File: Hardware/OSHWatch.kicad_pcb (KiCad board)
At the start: 4 copper layers, 30 x 36 mm, 46 parts, among them P1 CONN_30, U1 SPBT2632C2A.AT2, U10 DRV2605L, U2 STM32F072, U3 MCP73831T, U4 FAN5331, U5 TPS61200

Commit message: Initial layout complete
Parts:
- added C15: 22uF, SM0603, F.Cu at (30.9, 45.2)
- added C25: 100nF, SM0402, F.Cu at (17.5, 24.9)
- added C26: 1uF, SM0402, B.Cu at (40.9, 42.7)
- added CON1: USB-MINI-B, 10118192, F.Cu at (19.4, 52.2)
- added D1: 1N4148, SOD-523, B.Cu at (28.6, 30.7)
- added D2: 1N4148, SOD-523, B.Cu at (28.6, 29.3)
- added D3: BAT54T1G, SOD-123, B.Cu at (29.2, 19.4)
- added L1: 10uH, 2518, B.Cu at (33.1, 22.0)
- added L2: 4.7uH, 1.2A, 2518, F.Cu at (27.2, 42.0)
- added M1: DC_MOTOR, 2PAD, B.Cu at (39.2, 49.1)
- added OSC1: KD3270031, KD3270031, F.Cu at (38.6, 20.6)
- added P2: CONN_2, 2PAD, B.Cu at (29.6, 50.9)
- added P3: CONN_4, 4pin, F.Cu at (29.6, 52.7)
- added R17: 10K, SM0402, B.Cu at (28.3, 24.8)
- added R18: 10K, SM0402, B.Cu at (31.1, 16.0)
- added R19: 200k, SM0402, F.Cu at (19.3, 15.2)
- added R20: 10K, SM0402, F.Cu at (17.4, 37.8)
- added R21: 200k, SM0402, B.Cu at (40.9, 46.7)
- added R22: 200k, SM0402, B.Cu at (42.9, 45.7)
- added R23: 10K, SM0402, F.Cu at (16.6, 18.2)
- added R24: 10K, SM0402, F.Cu at (38.9, 15.6)
- added R25: 10K, SM0402, B.Cu at (35.2, 48.4)
- added R26: 10K, SM0402, F.Cu at (15.5, 18.2)
- added R27: 10K, SM0402, F.Cu at (37.6, 15.6)
- added R28: 10K, SM0402, B.Cu at (34.2, 48.4)
- added SW1: SW_PUSH, B3U-3000P, B.Cu at (18.5, 15.5)
- added SW2: SW_PUSH, B3U-3000P, B.Cu at (39.4, 15.5)
- added SW3: SW_PUSH, B3U-3000P, F.Cu at (39.5, 52.5)
- added U11: BMP280, BMP280, F.Cu at (16.6, 27.8)
- added U6: ML8511, ML8511, F.Cu at (22.9, 16.8)
- added U7: APDS-9960, APDS-9960, F.Cu at (29.5, 16.3)
- added U8: LSM9DS0, LSM9DS0, F.Cu at (20.4, 39.2)
- added U9: HTU21DF, HTU12DF, F.Cu at (20.6, 25.4)
- C1, C12, C14, C19, R13, R16, U10: moved to B.Cu
- C16: value 10uf -> 100uF; footprint SM0402 -> SM0805; moved to B.Cu
- C18: value 1uf -> 1nF
- C23: value 1uf -> 100nF
- C24: value 1uf -> 0.1uF; moved to B.Cu
- moved C21 34.2 mm to (22.6, 42.0)
- moved C10 33.6 mm to (15.6, 47.0), turned to 180 degrees
- moved R14 32.7 mm to (30.6, 47.2), turned to 180 degrees
- moved R1 32.3 mm to (16.6, 33.0)
- moved R2 31.7 mm to (18.3, 31.6)
- moved C24 30.8 mm to (36.8, 47.0), turned to 270 degrees
- moved C20 30.5 mm to (17.4, 39.6), turned to 270 degrees
- moved C13 29.8 mm to (30.5, 43.1)
- moved C11 27.4 mm to (26.3, 49.8), turned to 180 degrees
- moved R9 26.8 mm to (26.3, 48.6), turned to 180 degrees
- moved C22 26.4 mm to (20.7, 42.0), turned to 180 degrees
- moved U2 26.2 mm to (26.8, 33.0), turned to 270 degrees
- moved C23 24.9 mm to (15.9, 25.3), turned to 90 degrees
- moved C1 24.6 mm to (42.9, 40.9), turned to 270 degrees
- moved U4 19.1 mm to (29.6, 22.0), turned to 270 degrees
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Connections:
- C16 pad 1: +3.3V -> +BATT
- C19 pad 1: +3.3V -> +BATT
- R16 pad 1: N-00000104 -> N-0000027
- R16 pad 2: +3.3V -> /Bluetooth/BT_RESET
- R6 pad 1: +BATT -> N-0000028
- R6 pad 2: /Power/VBAT_SENSE -> /Bluetooth/32KHZ_CLK
- R7 pad 1: /Power/VBAT_SENSE -> N-0000028
- U1 pad 10: /Bluetooth/BT_RESET -> N-0000027
- U1 pad 11: /Bluetooth/BT_CTS_STM_RTS -> (no net)
- U1 pad 12: /Bluetooth/BT_RTS_STM_CTS -> (no net)
- U1 pad 15: (no net) -> N-0000028
- U2 pad 10: /Bluetooth/BT_RX_STM_TX -> /STM32F072/BUTTON_1
- U2 pad 11: /Bluetooth/BT_TX_STM_RX -> /STM32F072/UV_EN
- U2 pad 12: (no net) -> /Power/DISPLAY_BIAS_EN
- U2 pad 19: /STM32F072/GESTURE_INT -> /Display/DISPLAY_DC
- U2 pad 2: (no net) -> /STM32F072/GESTURE_INT
- U2 pad 20: /STM32F072/GYRO_INT -> /Display/DISPLAY_RESET
- U2 pad 28: (no net) -> /STM32F072/GYRO_INT
- U2 pad 29: /Power/DISPLAY_BIAS_EN -> /STM32F072/XM_INT
- U2 pad 34: (no net) -> N-0000041
- U2 pad 37: (no net) -> N-0000042
- U2 pad 38: /Bluetooth/BT_CTS_STM_RTS -> /STM32F072/BUTTON_3
- U2 pad 39: /Display/DISPLAY_RESET -> /STM32F072/BUTTON_2
- U2 pad 40: /Display/DISPLAY_DC -> (no net)
- U2 pad 41: /STM32F072/XM_INT -> (no net)
- U2 pad 42: /STM32F072/UV_EN -> /Bluetooth/BT_RX_STM_TX
- U2 pad 43: /Bluetooth/BT_RTS_STM_CTS -> /Bluetooth/BT_TX_STM_RX
- U2 pad 7: (no net) -> /STM32F072/NRST
- U4 pad 4: /Power/DISPLAY_BIAS_EN -> N-0000086
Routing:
- net +BATT: track 0.00 -> 117.7 mm, vias 0 -> 8
- net /STM32F072/I2C_SCK: track 0.00 -> 74.0 mm, vias 0 -> 4
- net /STM32F072/I2C_SDA: track 0.00 -> 67.7 mm, vias 0 -> 6
- net +3.3V: track 0.00 -> 60.8 mm, vias 0 -> 22
- net /STM32F072/NRST: track 0.00 -> 33.1 mm, vias 0 -> 1
- net /STM32F072/VIB_TRIG: track 0.00 -> 32.7 mm, vias 0 -> 2
- net /Bluetooth/BT_RESET: track 0.00 -> 30.0 mm, vias 0 -> 3
- net /STM32F072/BUTTON_2: track 0.00 -> 26.1 mm, vias 0 -> 2
- net /STM32F072/VIB_EN: track 0.00 -> 25.1 mm, vias 0 -> 2
- net /STM32F072/UV_OUT: track 0.00 -> 23.2 mm, vias 0 -> 2
- net /STM32F072/UV_EN: track 0.00 -> 21.1 mm, vias 0 -> 2
- net GND: track 0.00 -> 21.1 mm, vias 0 -> 8
- net /STM32F072/BUTTON_3: track 0.00 -> 20.7 mm, vias 0 -> 2
- net N-0000042: track 0.00 -> 20.6 mm, vias 0 -> 2
- net N-0000041: track 0.00 -> 19.6 mm
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- added copper zone on Inner1.Cu, net GND
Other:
- board size 30 x 36 mm -> 30 x 39.9 mm
- net class Default: trace_width 0.254 -> 0.2032; via_dia 0.889 -> 0.635; via_drill 0.635 -> 0.3048
- net class Power added: clearance 0.2, trace_width 0.254, via_dia 0.635, via_drill 0.3048
- rule trace_min: 0.254 -> 0.127
- rule via_min_drill: 0.508 -> 0.3048
- rule via_min_size: 0.889 -> 0.635

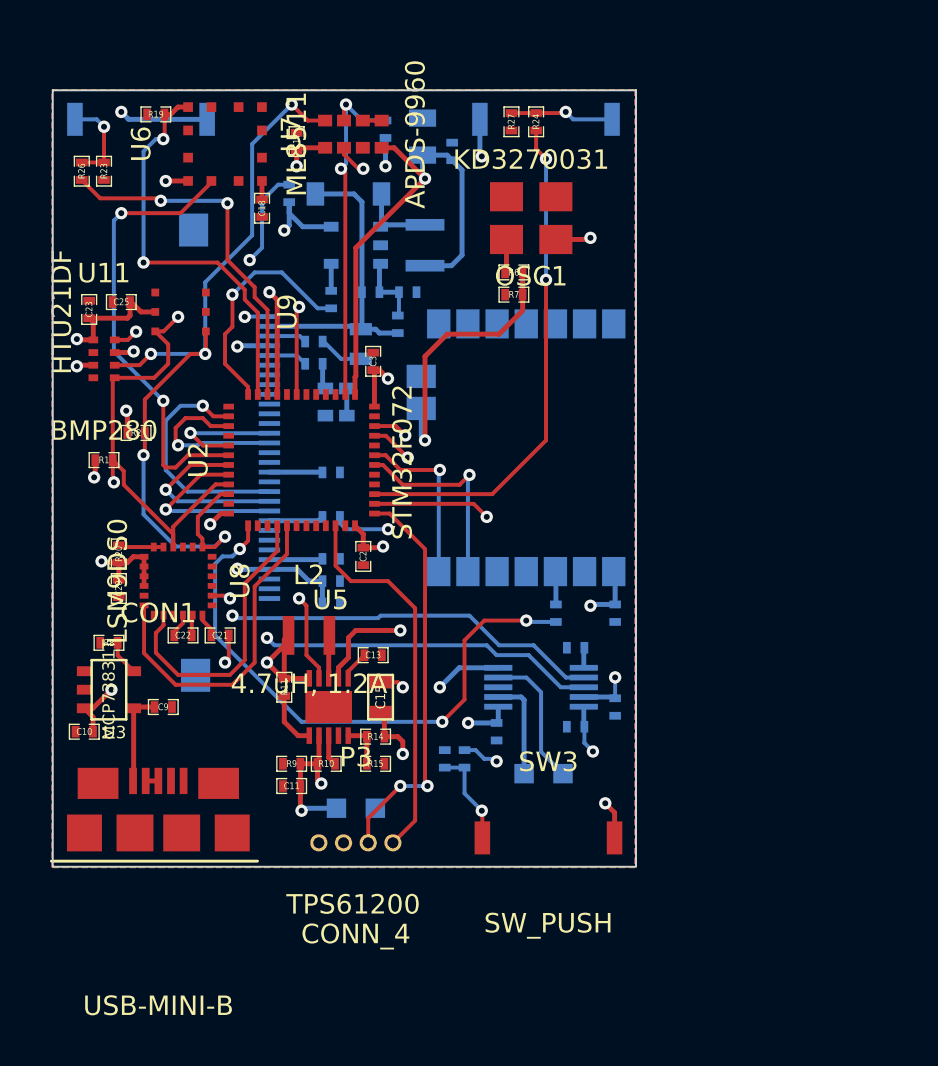
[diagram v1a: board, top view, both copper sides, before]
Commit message: Footprint corrections
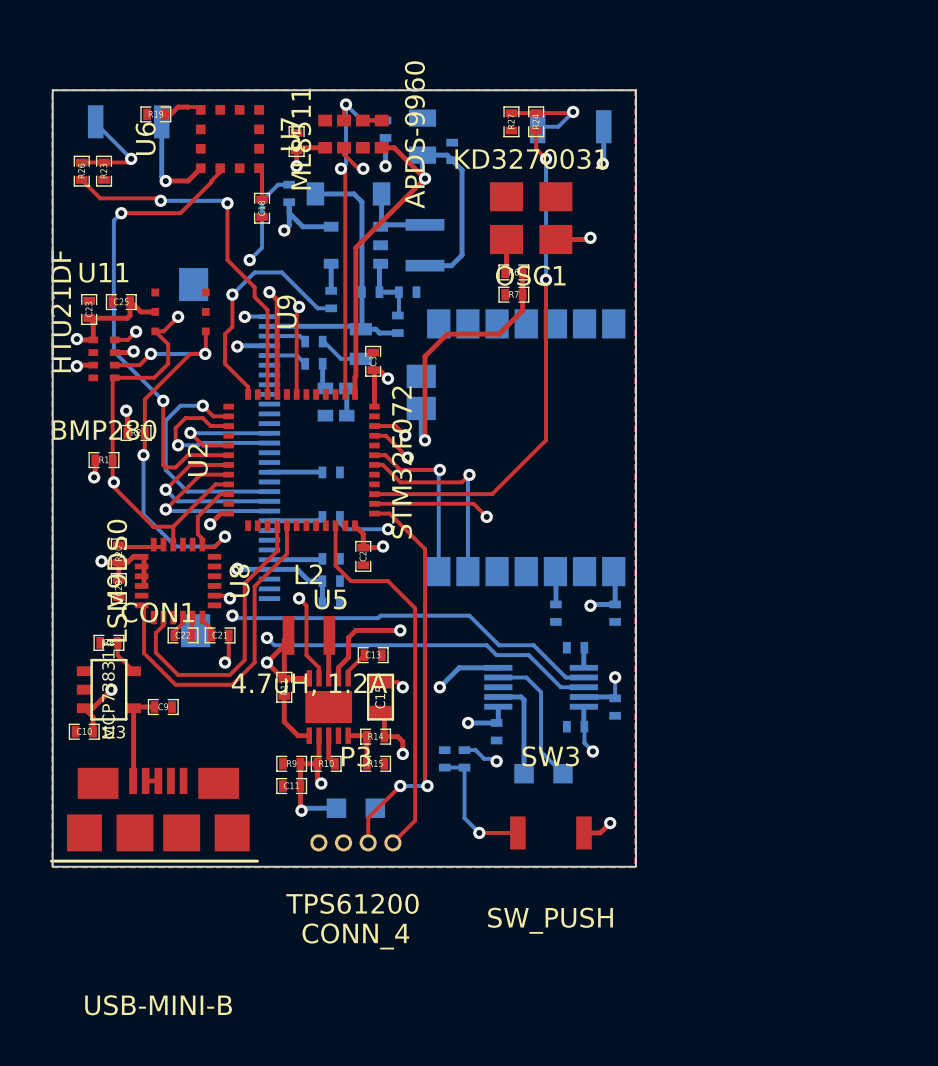
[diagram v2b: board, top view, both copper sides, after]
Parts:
- moved SW2 1.33 mm to (40.6, 15.9), turned to 180 degrees
- moved SW1 0.65 mm to (17.9, 15.6)
- moved U6 0.36 mm to (23.1, 16.5)
- moved SW3 0.28 mm to (39.6, 52.2)
- moved P1 0.25 mm to (25.1, 32.9)
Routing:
- net /Bluetooth/BT_RESET: track 30.0 -> 0.00 mm, vias 3 -> 0
- net /STM32F072/UV_EN: track 21.1 -> 2.08 mm, vias 2 -> 0
- net /STM32F072/I2C_SDA: track 67.7 -> 50.9 mm, vias 6 -> 5
- net N-0000099: track 5.01 -> 6.68 mm
- net /STM32F072/I2C_SCK: track 74.0 -> 72.4 mm
- net +3.3V: track 60.8 -> 59.8 mm, vias 22 -> 21
- net /STM32F072/UV_OUT: track 23.2 -> 24.0 mm
- net N-0000095: track 0.95 -> 1.67 mm
- net N-00000100: track 4.63 -> 5.28 mm

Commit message: Final footprint corrections, gerbers
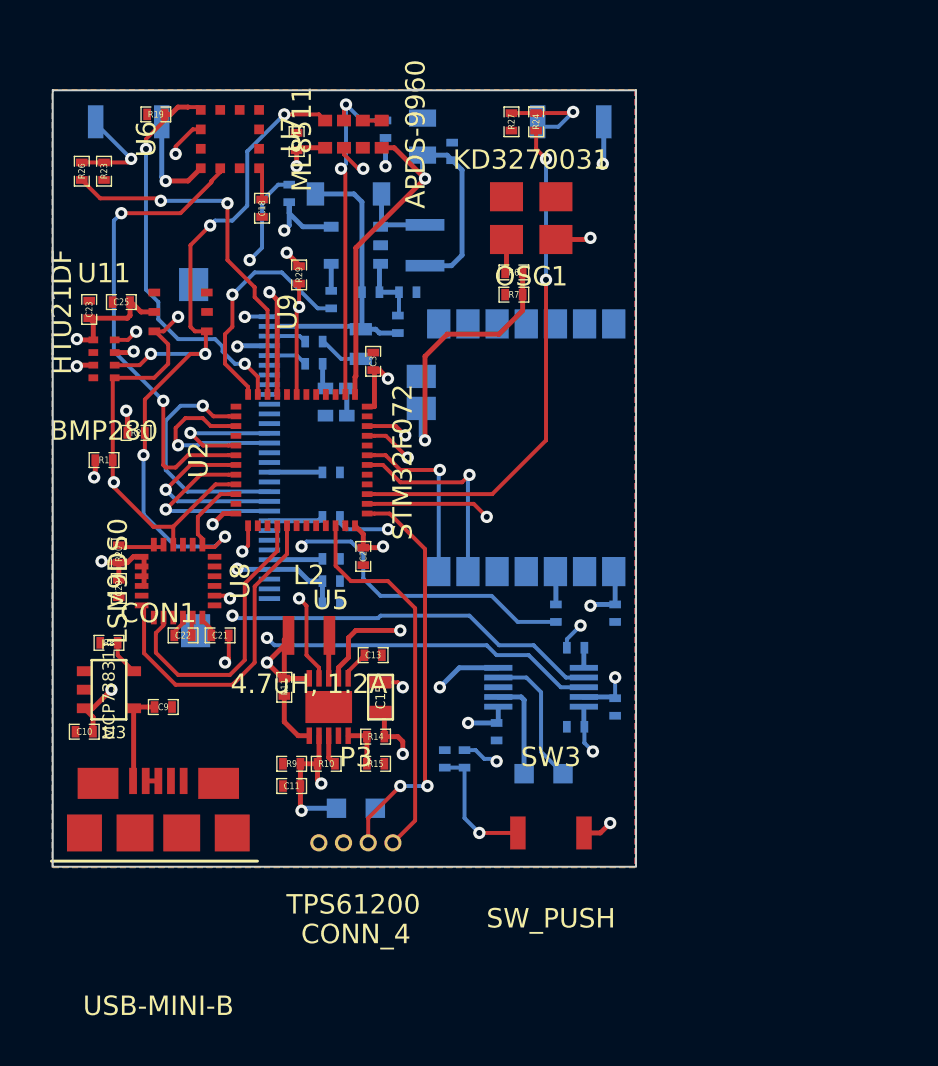
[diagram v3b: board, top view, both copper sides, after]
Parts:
- added R29: 10K, SM0402, F.Cu at (26.7, 23.5)
- moved SW2 0.25 mm to (40.6, 15.6)
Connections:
- U2 pad 44: (no net) -> GND
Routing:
- net /Bluetooth/BT_RESET: track 0.00 -> 20.2 mm, vias 0 -> 2
- net /STM32F072/UV_EN: track 2.08 -> 20.7 mm, vias 0 -> 2
- net /STM32F072/I2C_SDA: track 50.9 -> 67.9 mm, vias 5 -> 7
- net GND: track 21.1 -> 24.6 mm, vias 8 -> 10
- net +3.3V: track 59.8 -> 61.4 mm, vias 21 -> 22
- net /STM32F072/NRST: track 33.1 -> 34.3 mm

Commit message: Rev X1 Gerbers
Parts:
- moved C22 0.25 mm to (20.7, 42.3)
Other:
- board text added: "."
- board text added: "REV X1"
- board text added: "voidptr.org/oshwatch"
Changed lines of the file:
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@@
     (area 13.028667 10.446 55.168715 61.872)
     (thickness 1.6)
-    (drawings 6)
+    (drawings 17)
     (tracks 637)
     (zones 0)
@@
     (19 F.Paste user hide)
     (20 B.SilkS user)
-    (21 F.SilkS user hide)
+    (21 F.SilkS user)
     (22 B.Mask user)
     (23 F.Mask user hide)
@@
   )
   (module SM0402 (layer F.Cu)
-    (at 20.701 42.037 180)
+    (at 20.701 42.291 180)
     (attr smd)
     (fp_text reference C22 (at 0 0 180) (layer F.SilkS)
@@
     )
   )
+  (gr_text "REV X1" (at 40.386 32.131 90) (layer F.SilkS)
+    (effects (font (size 1.5 1.5) (thickness 0.3)))
+  )
+  (gr_text . (at 29.21 42.672) (layer F.SilkS)
+    (effects (font (size 1.5 1.5) (thickness 0.3)))
+  )
+  (gr_text . (at 42.545 42.545) (layer B.SilkS)
+    (effects (font (size 1.5 1.5) (thickness 0.3)) (justify mirror))
+  )
+  (gr_text . (at 26.924 14.478) (layer F.SilkS)
+    (effects (font (size 1.5 1.5) (thickness 0.3)))
+  )
+  (gr_text . (at 41.783 18.161) (layer F.SilkS)
+    (effects (font (size 1.5 1.5) (thickness 0.3)))
+  )
+  (gr_text . (at 25.4 15.24) (layer F.SilkS)
+    (effects (font (size 1.5 1.5) (thickness 0.3)))
+  )
+  (gr_text . (at 22.733 25.908) (layer F.SilkS)
+    (effects (font (size 1.5 1.5) (thickness 0.3)))
+  )
+  (gr_text . (at 17.653 25.527) (layer F.SilkS)
+    (effects (font (size 1.5 1.5) (thickness 0.3)))
+  )
+  (gr_text . (at 23.114 37.338) (layer F.SilkS)
+    (effects (font (size 1.5 1.5) (thickness 0.3)))
+  )
+  (gr_text . (at 30.353 28.956) (layer F.SilkS)
+    (effects (font (size 1.5 1.5) (thickness 0.3)))
+  )
+  (gr_text voidptr.org/oshwatch (at 42.545 32.004 90) (layer F.SilkS)
+    (effects (font (size 1.5 1.5) (thickness 0.3)))
+  )
   (dimension 39.878 (width 0.3) (layer Dwgs.User)
     (gr_text "1.5700 in" (at 49.483 33.909 90) (layer Dwgs.User)
@@
   (via (at 29.083 14.732) (size 0.635) (layers F.Cu B.Cu) (net 18))
   (segment (start 28.979 14.836) (end 29.083 14.732) (width 0.2032) (layer F.Cu) (net 18))
-  (segment (start 19.697 40.993) (end 19.697 41.517) (width 0.2032) (layer F.Cu) (net 19))
+  (segment (start 19.697 40.993) (end 19.697 41.644) (width 0.2032) (layer F.Cu) (net 19))
   (segment (start 25.547 37.699) (end 25.547 36.395) (width 0.2032) (layer F.Cu) (net 19))
   (segment (start 23.876 39.37) (end 25.547 37.699) (width 0.2032) (layer F.Cu) (net 19))
@@
   (segment (start 20.447 44.069) (end 23.114 44.069) (width 0.2032) (layer F.Cu) (net 19))
   (segment (start 19.304 42.926) (end 20.447 44.069) (width 0.2032) (layer F.Cu) (net 19))
-  (segment (start 19.304 41.91) (end 19.304 42.926) (width 0.2032) (layer F.Cu) (net 19))
-  (segment (start 19.697 41.517) (end 19.304 41.91) (width 0.2032) (layer F.Cu) (net 19))
+  (segment (start 19.304 42.037) (end 19.304 42.926) (width 0.2032) (layer F.Cu) (net 19))
+  (segment (start 19.697 41.644) (end 19.304 42.037) (width 0.2032) (layer F.Cu) (net 19))
   (segment (start 23.422 34.27) (end 23.047 34.27) (width 0.2032) (layer F.Cu) (net 20))
   (segment (start 20.197 36.445) (end 20.197 36.449) (width 0.2032) (layer F.Cu) (net 20))
@@
   (segment (start 23.422 34.77) (end 23.047 34.77) (width 0.2032) (layer F.Cu) (net 21))
   (segment (start 22.634 34.77) (end 21.463 35.941) (width 0.2032) (layer F.Cu) (net 21))
-  (segment (start 21.463 35.941) (end 21.463 36.83) (width 0.2032) (layer F.Cu) (net 21))
-  (segment (start 21.463 36.83) (end 21.697 37.064) (width 0.2032) (layer F.Cu) (net 21))
-  (segment (start 21.697 37.064) (end 21.697 37.493) (width 0.2032) (layer F.Cu) (net 21))
+  (segment (start 21.463 35.941) (end 21.463 36.576) (width 0.2032) (layer F.Cu) (net 21))
+  (segment (start 21.463 36.576) (end 21.697 36.81) (width 0.2032) (layer F.Cu) (net 21))
+  (segment (start 21.697 36.81) (end 21.697 37.493) (width 0.2032) (layer F.Cu) (net 21))
   (segment (start 23.047 34.77) (end 22.634 34.77) (width 0.2032) (layer F.Cu) (net 21))
   (segment (start 22.324 37.493) (end 22.86 36.957) (width 0.2032) (layer F.Cu) (net 21))
@@
   (segment (start 24.384 39.519202) (end 24.384 43.434) (width 0.2032) (layer F.Cu) (net 27))
   (segment (start 26.047 37.856202) (end 24.384 39.519202) (width 0.2032) (layer F.Cu) (net 27))
-  (segment (start 40.44442 42.672) (end 40.44442 42.23258) (width 0.2032) (layer B.Cu) (net 28) (status 400000))
+  (segment (start 40.44442 42.672) (end 40.44442 42.23258) (width 0.2032) (layer B.Cu) (net 28))
   (via (at 41.148 41.529) (size 0.635) (layers F.Cu B.Cu) (net 28))
   (segment (start 40.44442 42.23258) (end 41.148 41.529) (width 0.2032) (layer B.Cu) (net 28))
@@
   (segment (start 22.15642 41.71442) (end 22.15642 42.037) (width 0.2032) (layer F.Cu) (net 29))
   (segment (start 21.697 41.255) (end 22.15642 41.71442) (width 0.2032) (layer F.Cu) (net 29))
-  (segment (start 21.15058 42.037) (end 21.15058 41.03942) (width 0.2032) (layer F.Cu) (net 30))
-  (segment (start 21.15058 41.03942) (end 21.197 40.993) (width 0.2032) (layer F.Cu) (net 30))
+  (segment (start 21.15058 42.291) (end 21.15058 41.16442) (width 0.2032) (layer F.Cu) (net 30))
+  (segment (start 21.15058 41.16442) (end 21.197 41.118) (width 0.2032) (layer F.Cu) (net 30))
   (segment (start 29.949 15.556) (end 30.919 15.556) (width 0.2032) (layer F.Cu) (net 31))
-  (segment (start 20.25142 42.037) (end 20.25142 41.85158) (width 0.2032) (layer F.Cu) (net 32))
-  (segment (start 20.697 41.406) (end 20.697 40.993) (width 0.2032) (layer F.Cu) (net 32))
-  (segment (start 20.25142 41.85158) (end 20.697 41.406) (width 0.2032) (layer F.Cu) (net 32))
+  (segment (start 20.25142 42.291) (end 20.25142 42.23258) (width 0.2032) (layer F.Cu) (net 32))
+  (segment (start 20.697 41.787) (end 20.697 41.118) (width 0.2032) (layer F.Cu) (net 32))
+  (segment (start 20.25142 42.23258) (end 20.697 41.787) (width 0.2032) (layer F.Cu) (net 32))
   (segment (start 39.878 40.44442) (end 39.878 38.779) (width 0.254) (layer B.Cu) (net 33))
   (segment (start 39.878 38.779) (end 39.854 38.755) (width 0.254) (layer B.Cu) (net 33))
